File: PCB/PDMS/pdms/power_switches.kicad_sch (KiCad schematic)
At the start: 0 parts

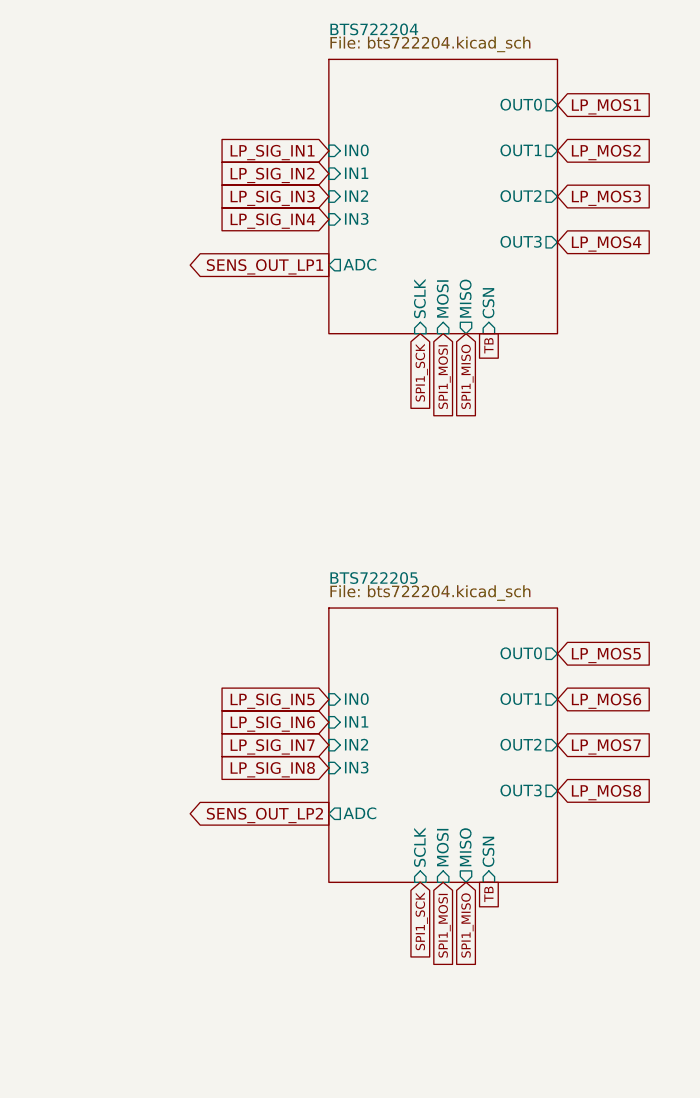
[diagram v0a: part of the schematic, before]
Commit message: Changed MCU to L496 & finished powerswitch section
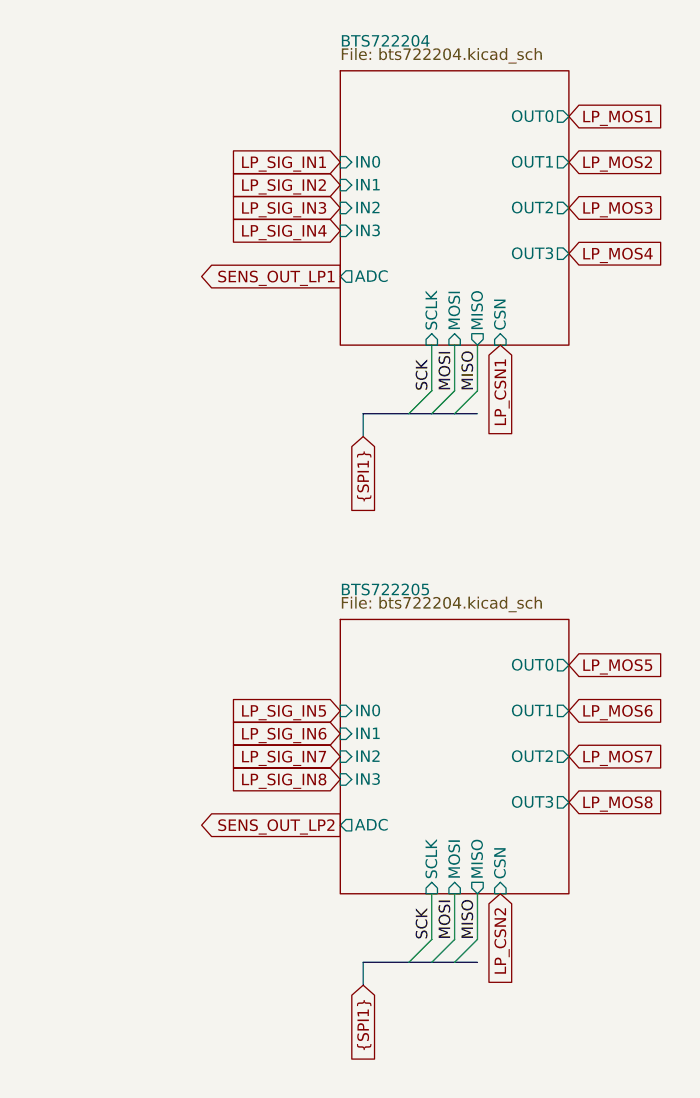
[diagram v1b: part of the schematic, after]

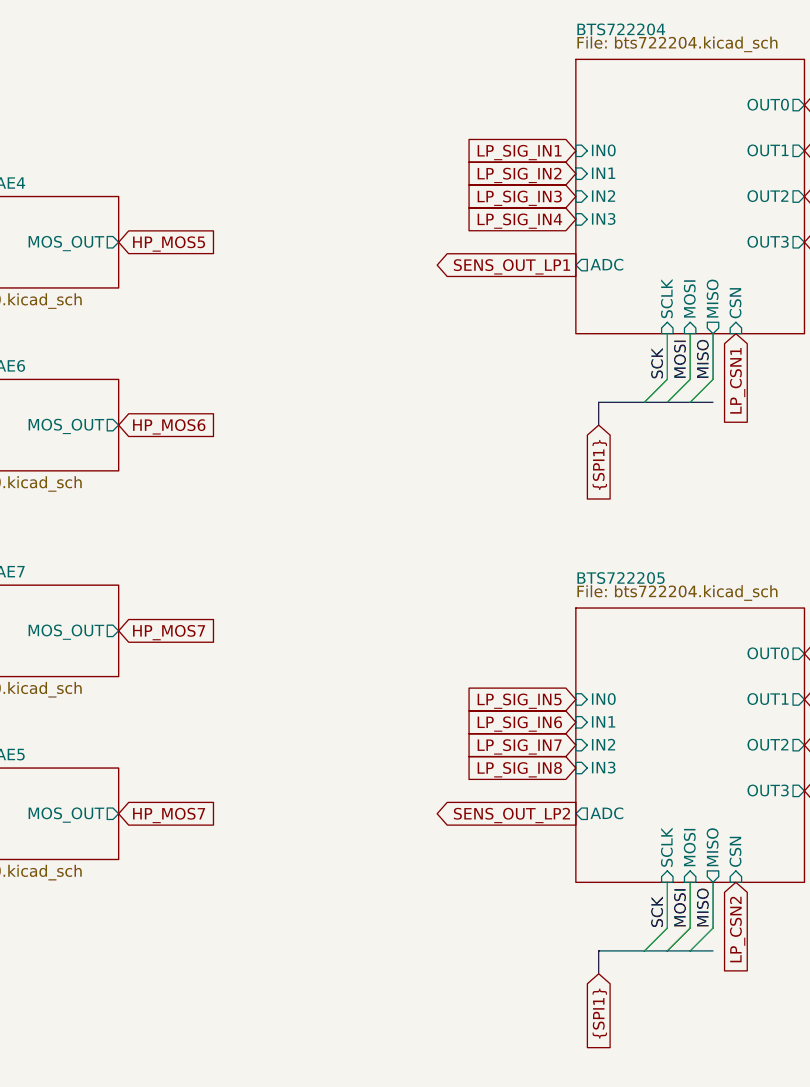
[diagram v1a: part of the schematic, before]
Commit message: Wired all peripherals
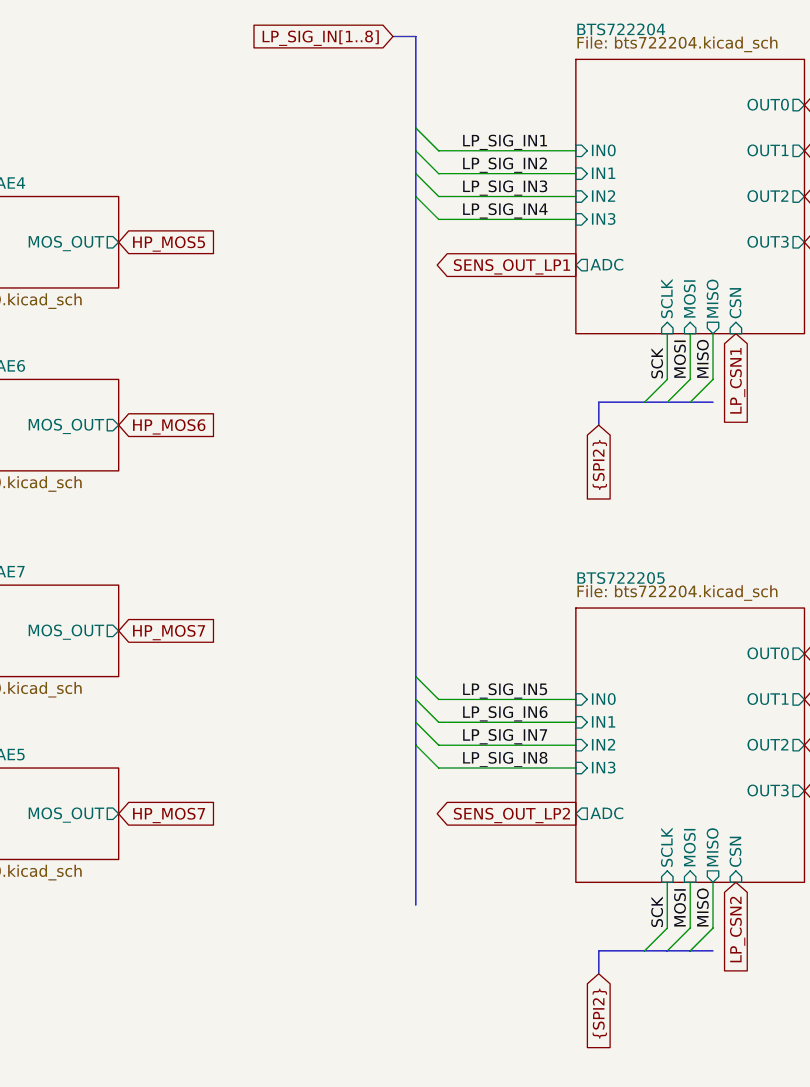
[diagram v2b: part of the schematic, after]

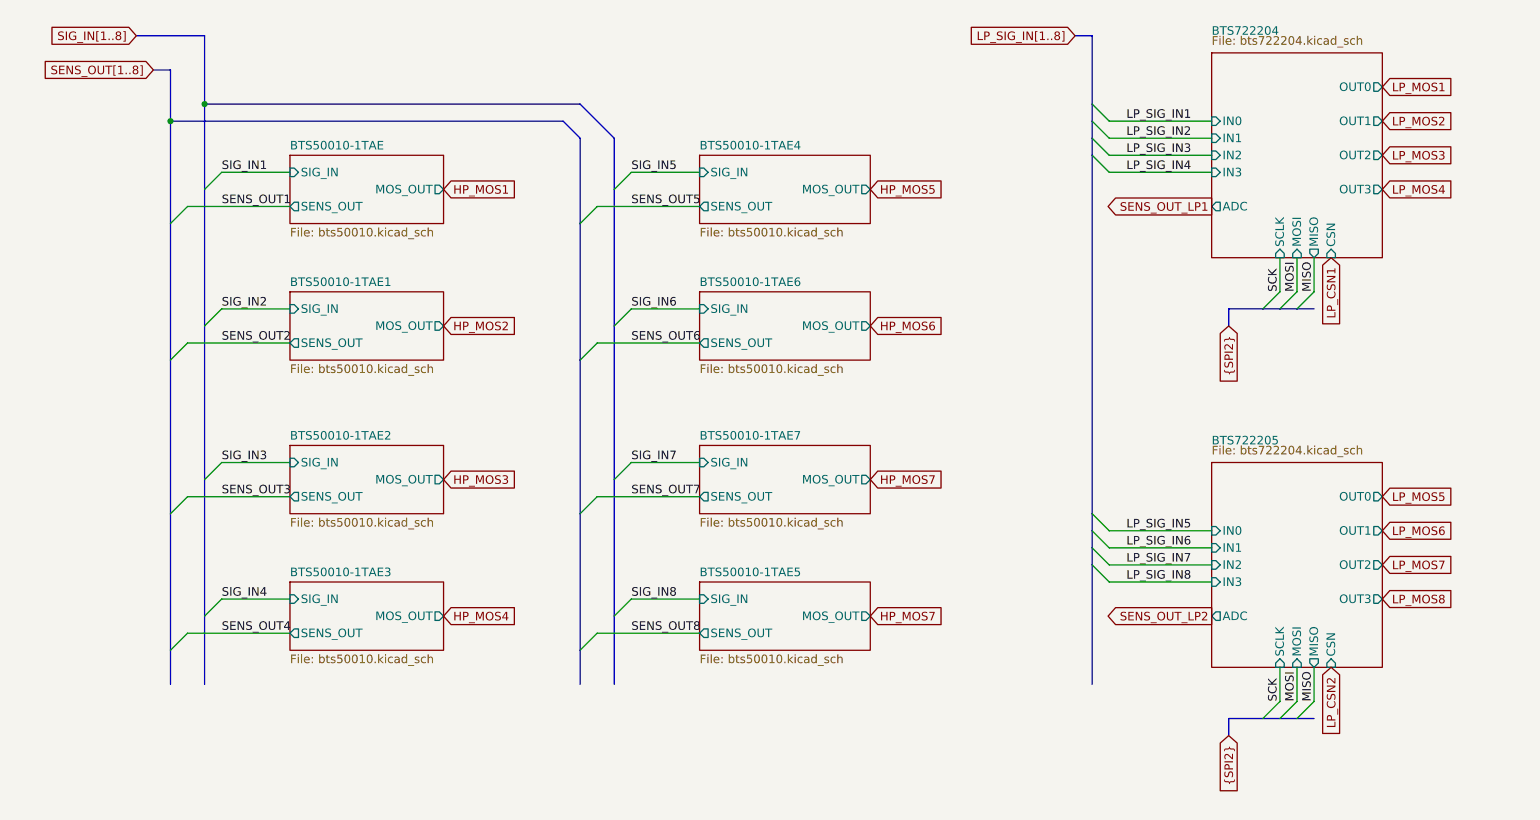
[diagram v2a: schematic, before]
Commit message: Added input selection section and fusing
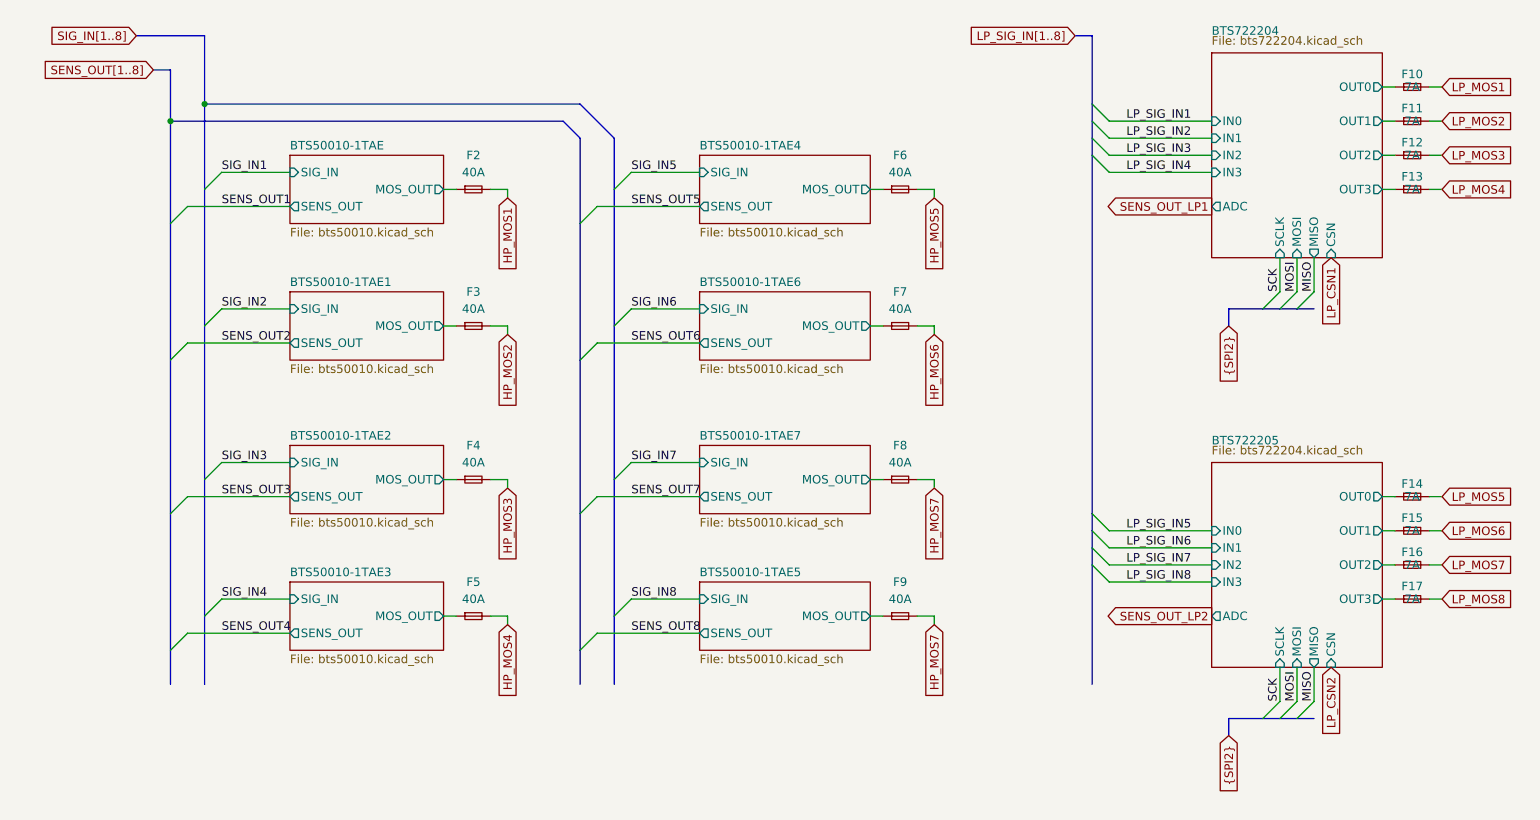
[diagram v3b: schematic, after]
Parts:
- added F10, F11, F12, F13, F14, F15, F16, F17: 7A, symbol Device:Fuse_Small
- added F2, F3, F4, F5, F6, F7, F8, F9: 40A, symbol Device:Fuse_Small
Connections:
- net HP_MOS1: now also F2.2
- net HP_MOS2: now also F3.2
- net HP_MOS3: now also F4.2
- net HP_MOS4: now also F5.2
- net HP_MOS5: now also F6.2
- net HP_MOS6: now also F7.2
- net HP_MOS7: now also F8.2, F9.2
- net LP_MOS1: now also F10.2
- net LP_MOS2: now also F11.2
- net LP_MOS3: now also F12.2
- net LP_MOS4: now also F13.2
- net LP_MOS5: now also F14.2
- net LP_MOS6: now also F15.2
- net LP_MOS7: now also F16.2
- net LP_MOS8: now also F17.2
- new net BTS50010-1TAE/MOS_OUT: F2.1
- new net BTS50010-1TAE1/MOS_OUT: F3.1
- new net BTS50010-1TAE2/MOS_OUT: F4.1
- new net BTS50010-1TAE3/MOS_OUT: F5.1
- new net BTS50010-1TAE4/MOS_OUT: F6.1
- new net BTS50010-1TAE5/MOS_OUT: F9.1
- new net BTS50010-1TAE6/MOS_OUT: F7.1
- new net BTS50010-1TAE7/MOS_OUT: F8.1
- new net BTS722204/OUT0: F10.1
- new net BTS722204/OUT1: F11.1
- new net BTS722204/OUT2: F12.1
- new net BTS722204/OUT3: F13.1
- new net BTS722205/OUT0: F14.1
- new net BTS722205/OUT1: F15.1
- new net BTS722205/OUT2: F16.1
- new net BTS722205/OUT3: F17.1

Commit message: Mostly assigned footprints
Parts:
- F10, F11, F12, F13, F14, F15, F16, F17: footprint (none) -> Fuse:Fuse_1206_3216Metric
- F2, F3, F4, F5, F6, F7, F8, F9: footprint (none) -> PDMS_Additional:0ACA9400TE
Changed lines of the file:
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@@
     (property "Reference" "F11" (id 0) (at 233.045 56.515 0))
     (property "Value" "7A" (id 1) (at 233.045 58.42 0))
-    (property "Footprint" "" (id 2) (at 233.045 58.42 0)
+    (property "Footprint" "Fuse:Fuse_1206_3216Metric" (id 2) (at 233.045 58.42 0)
       (effects (font (size 1.27 1.27)) hide)
     )
@@
     (property "Reference" "F4" (id 0) (at 93.345 106.68 0))
     (property "Value" "40A" (id 1) (at 93.345 109.22 0))
-    (property "Footprint" "" (id 2) (at 93.345 111.76 0)
+    (property "Footprint" "PDMS_Additional:0ACA9400TE" (id 2) (at 93.345 111.76 0)
       (effects (font (size 1.27 1.27)) hide)
     )
@@
     (property "Reference" "F5" (id 0) (at 93.345 127 0))
     (property "Value" "40A" (id 1) (at 93.345 129.54 0))
-    (property "Footprint" "" (id 2) (at 93.345 132.08 0)
+    (property "Footprint" "PDMS_Additional:0ACA9400TE" (id 2) (at 93.345 132.08 0)
       (effects (font (size 1.27 1.27)) hide)
     )
@@
     (property "Reference" "F12" (id 0) (at 233.045 61.595 0))
     (property "Value" "7A" (id 1) (at 233.045 63.5 0))
-    (property "Footprint" "" (id 2) (at 233.045 63.5 0)
+    (property "Footprint" "Fuse:Fuse_1206_3216Metric" (id 2) (at 233.045 63.5 0)
       (effects (font (size 1.27 1.27)) hide)
     )
@@
     (property "Reference" "F14" (id 0) (at 233.045 112.395 0))
     (property "Value" "7A" (id 1) (at 233.045 114.3 0))
-    (property "Footprint" "" (id 2) (at 233.045 114.3 0)
+    (property "Footprint" "Fuse:Fuse_1206_3216Metric" (id 2) (at 233.045 114.3 0)
       (effects (font (size 1.27 1.27)) hide)
     )
@@
     (property "Reference" "F8" (id 0) (at 156.845 106.68 0))
     (property "Value" "40A" (id 1) (at 156.845 109.22 0))
-    (property "Footprint" "" (id 2) (at 156.845 111.76 0)
+    (property "Footprint" "PDMS_Additional:0ACA9400TE" (id 2) (at 156.845 111.76 0)
       (effects (font (size 1.27 1.27)) hide)
     )
@@
     (property "Reference" "F13" (id 0) (at 233.045 66.675 0))
     (property "Value" "7A" (id 1) (at 233.045 68.58 0))
-    (property "Footprint" "" (id 2) (at 233.045 68.58 0)
+    (property "Footprint" "Fuse:Fuse_1206_3216Metric" (id 2) (at 233.045 68.58 0)
       (effects (font (size 1.27 1.27)) hide)
     )
@@
     (property "Reference" "F7" (id 0) (at 156.845 83.82 0))
     (property "Value" "40A" (id 1) (at 156.845 86.36 0))
-    (property "Footprint" "" (id 2) (at 156.845 88.9 0)
+    (property "Footprint" "PDMS_Additional:0ACA9400TE" (id 2) (at 156.845 88.9 0)
       (effects (font (size 1.27 1.27)) hide)
     )
@@
     (property "Reference" "F17" (id 0) (at 233.045 127.635 0))
     (property "Value" "7A" (id 1) (at 233.045 129.54 0))
-    (property "Footprint" "" (id 2) (at 233.045 129.54 0)
+    (property "Footprint" "Fuse:Fuse_1206_3216Metric" (id 2) (at 233.045 129.54 0)
       (effects (font (size 1.27 1.27)) hide)
     )
@@
     (property "Reference" "F3" (id 0) (at 93.345 83.82 0))
     (property "Value" "40A" (id 1) (at 93.345 86.36 0))
-    (property "Footprint" "" (id 2) (at 93.345 88.9 0)
+    (property "Footprint" "PDMS_Additional:0ACA9400TE" (id 2) (at 93.345 88.9 0)
       (effects (font (size 1.27 1.27)) hide)
     )
@@
     (property "Reference" "F9" (id 0) (at 156.845 127 0))
     (property "Value" "40A" (id 1) (at 156.845 129.54 0))
-    (property "Footprint" "" (id 2) (at 156.845 132.08 0)
+    (property "Footprint" "PDMS_Additional:0ACA9400TE" (id 2) (at 156.845 132.08 0)
       (effects (font (size 1.27 1.27)) hide)
     )
@@
     (property "Reference" "F10" (id 0) (at 233.045 51.435 0))
     (property "Value" "7A" (id 1) (at 233.045 53.34 0))
-    (property "Footprint" "" (id 2) (at 233.045 53.34 0)
+    (property "Footprint" "Fuse:Fuse_1206_3216Metric" (id 2) (at 233.045 53.34 0)
       (effects (font (size 1.27 1.27)) hide)
     )
@@
     (property "Reference" "F15" (id 0) (at 233.045 117.475 0))
     (property "Value" "7A" (id 1) (at 233.045 119.38 0))
-    (property "Footprint" "" (id 2) (at 233.045 119.38 0)
+    (property "Footprint" "Fuse:Fuse_1206_3216Metric" (id 2) (at 233.045 119.38 0)
       (effects (font (size 1.27 1.27)) hide)
     )
@@
     (property "Reference" "F16" (id 0) (at 233.045 122.555 0))
     (property "Value" "7A" (id 1) (at 233.045 124.46 0))
-    (property "Footprint" "" (id 2) (at 233.045 124.46 0)
+    (property "Footprint" "Fuse:Fuse_1206_3216Metric" (id 2) (at 233.045 124.46 0)
       (effects (font (size 1.27 1.27)) hide)
     )
@@
     (property "Reference" "F2" (id 0) (at 93.345 63.5 0))
     (property "Value" "40A" (id 1) (at 93.345 66.04 0))
-    (property "Footprint" "" (id 2) (at 93.345 68.58 0)
+    (property "Footprint" "PDMS_Additional:0ACA9400TE" (id 2) (at 93.345 68.58 0)
       (effects (font (size 1.27 1.27)) hide)
     )
@@
     (property "Reference" "F6" (id 0) (at 156.845 63.5 0))
     (property "Value" "40A" (id 1) (at 156.845 66.04 0))
-    (property "Footprint" "" (id 2) (at 156.845 68.58 0)
-      (effects (font (size 1.27 1.27)) hide)
-    )
+    (property "Footprint" "PDMS_Additional:0ACA9400TE" (id 2) (at 156.845 68.58 0)
+      (effects (font (size 1.27 1.27)) hide)
+    )

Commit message: Crucial fully assigned schematics
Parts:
- removed F2, F3, F4, F5, F6, F7, F8, F9: 40A, PDMS_Additional:0ACA9400TE, symbol Device:Fuse_Small

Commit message: Welcome back
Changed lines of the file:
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@@
     )
   )
-  (global_label "HP_MOS7" (shape input) (at 154.305 132.08 0) (fields_autoplaced)
+  (global_label "HP_MOS8" (shape input) (at 154.305 132.08 0) (fields_autoplaced)
     (effects (font (size 1.27 1.27)) (justify left))
     (property "Intersheet References" "${INTERSHEET_REFS}" (id 0) (at 165.4871 132.0006 0)

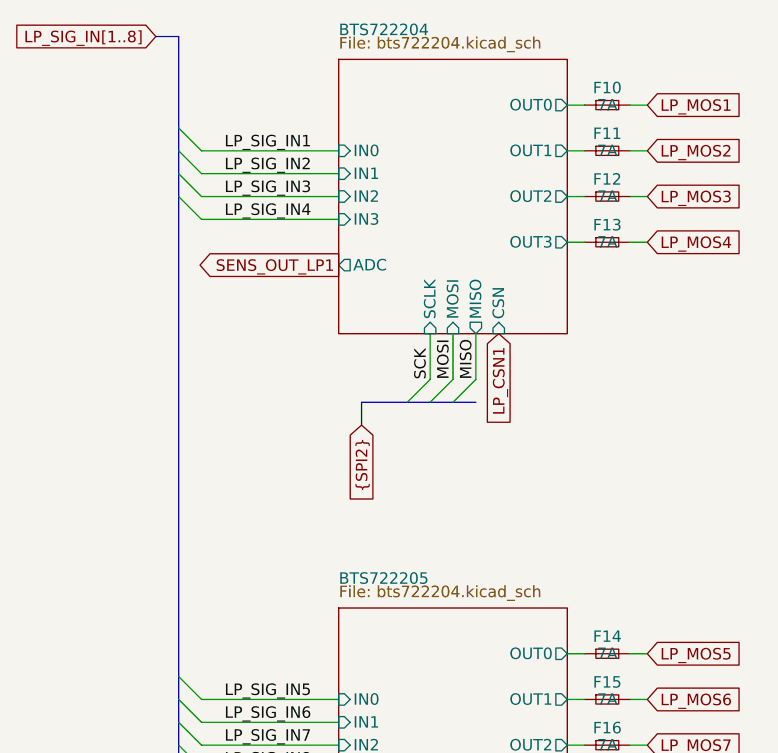
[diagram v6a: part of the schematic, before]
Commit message: Medium power stage layout
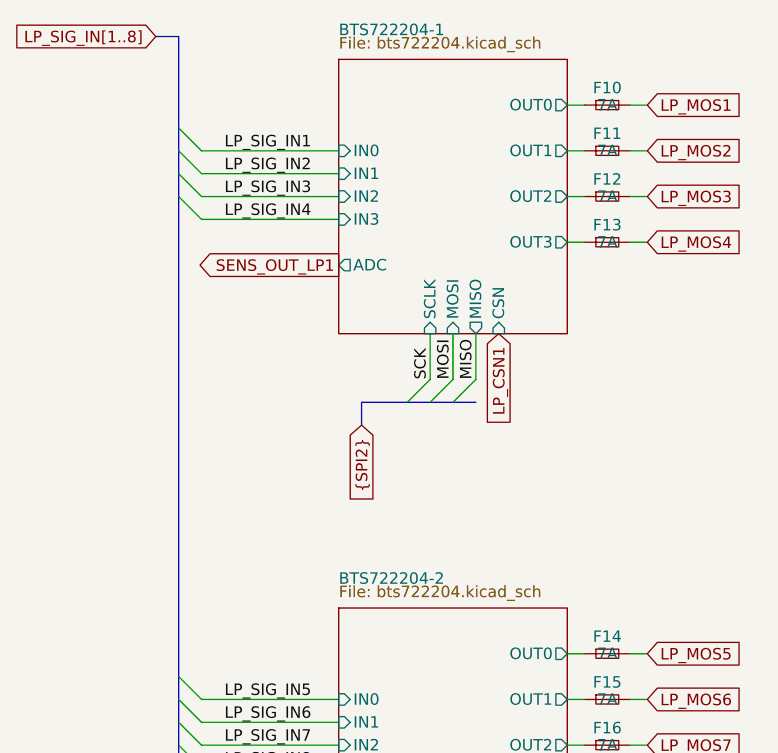
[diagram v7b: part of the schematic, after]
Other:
- sheet BTS722204 renamed BTS722204-1
- sheet BTS722205 renamed BTS722204-2
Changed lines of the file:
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@@
     (stroke (width 0.1524) (type solid) (color 0 0 0 0))
     (fill (color 0 0 0 0.0000))
-    (property "Sheet name" "BTS722204" (id 0) (at 203.2 45.72 0)
+    (property "Sheet name" "BTS722204-1" (id 0) (at 203.2 45.72 0)
       (effects (font (size 1.27 1.27)) (justify left bottom))
     )
@@
     (stroke (width 0.1524) (type solid) (color 0 0 0 0))
     (fill (color 0 0 0 0.0000))
-    (property "Sheet name" "BTS722205" (id 0) (at 203.2 106.68 0)
+    (property "Sheet name" "BTS722204-2" (id 0) (at 203.2 106.68 0)
       (effects (font (size 1.27 1.27)) (justify left bottom))
     )
